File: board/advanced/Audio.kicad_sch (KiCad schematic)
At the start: 12 parts, among them J10 AudioJack3, U9 PCM5102A

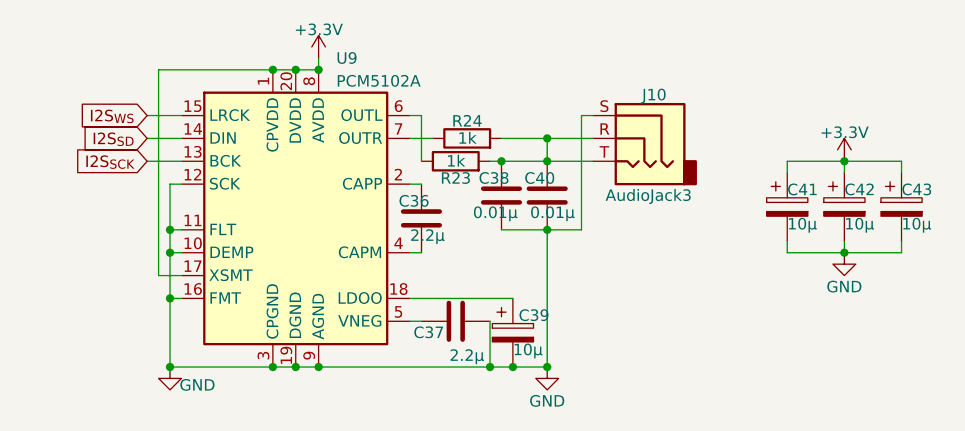
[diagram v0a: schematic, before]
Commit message: put footprints and change schematics
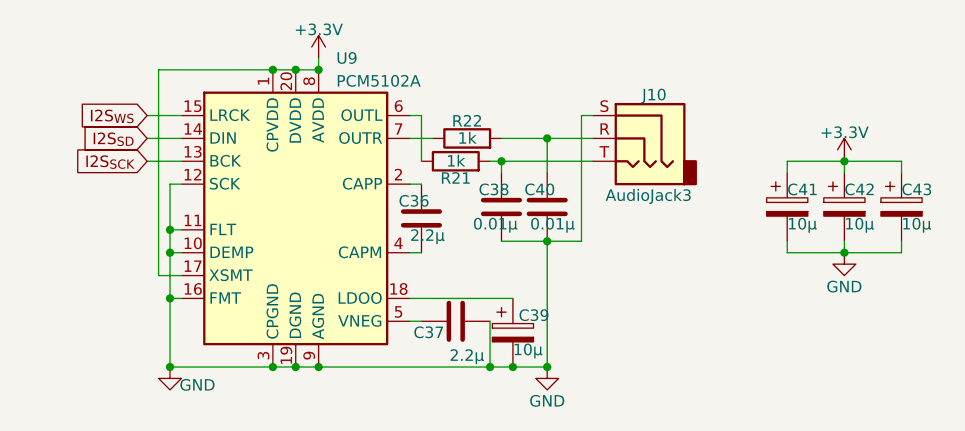
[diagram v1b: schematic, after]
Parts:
- R21: renamed from R23; footprint Resistor_SMD:R_0603_1608Metric -> Resistor_SMD:R_0402_1005Metric
- R22: renamed from R24; footprint Resistor_SMD:R_0603_1608Metric -> Resistor_SMD:R_0402_1005Metric
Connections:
- net at C40.1, J10.R, R22.2: no longer C38.1, J10.T, R21.2
- new net: C38.1, J10.T, R21.2
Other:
- moved on the sheet: C38, C40
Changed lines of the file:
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@@
-	)
-	(junction
-		(at 144.78 99.06)
-		(diameter 0)
-		(color 0 0 0 0)
 	)
 	(junction
@@
 	)
 	(junction
+		(at 144.78 107.95)
+		(diameter 0)
+		(color 0 0 0 0)
+	)
+	(junction
 		(at 114.3 88.9)
 		(diameter 0)
@@
 	)
 	(junction
-		(at 144.78 106.68)
+		(at 114.3 121.92)
+		(diameter 0)
+		(color 0 0 0 0)
+	)
+	(junction
+		(at 102.87 121.92)
+		(diameter 0)
+		(color 0 0 0 0)
+	)
+	(junction
+		(at 144.78 96.52)
 		(diameter 0)
 		(color 0 0 0 0)
@@
 	)
 	(junction
-		(at 114.3 121.92)
-		(diameter 0)
-		(color 0 0 0 0)
-	)
-	(junction
-		(at 102.87 121.92)
-		(diameter 0)
-		(color 0 0 0 0)
-	)
-	(junction
-		(at 144.78 96.52)
-		(diameter 0)
-		(color 0 0 0 0)
-	)
-	(junction
 		(at 102.87 109.22)
 		(diameter 0)
@@
 	(wire
 		(pts
-			(xy 144.78 106.68) (xy 144.78 121.92)
-		)
-		(stroke
-			(width 0)
-			(type default)
-		)
-	)
-	(wire
-		(pts
-			(xy 144.78 106.68) (xy 148.59 106.68)
+			(xy 148.59 107.95) (xy 144.78 107.95)
+		)
+		(stroke
+			(width 0)
+			(type default)
+		)
+	)
+	(wire
+		(pts
+			(xy 144.78 107.95) (xy 144.78 121.92)
 		)
 		(stroke
@@
 	(wire
 		(pts
-			(xy 148.59 93.98) (xy 148.59 106.68)
+			(xy 148.59 93.98) (xy 148.59 107.95)
 		)
 		(stroke
@@
 	(wire
 		(pts
-			(xy 144.78 99.06) (xy 149.86 99.06)
-		)
-		(stroke
-			(width 0)
-			(type default)
-		)
-	)
-	(wire
-		(pts
 			(xy 129.54 96.52) (xy 132.08 96.52)
 		)
@@
 	(wire
 		(pts
-			(xy 139.7 106.68) (xy 144.78 106.68)
+			(xy 139.7 100.33) (xy 139.7 99.06)
+		)
+		(stroke
+			(width 0)
+			(type default)
+		)
+	)
+	(wire
+		(pts
+			(xy 139.7 107.95) (xy 144.78 107.95)
 		)
 		(stroke
@@
 	(wire
 		(pts
-			(xy 139.7 99.06) (xy 144.78 99.06)
-		)
-		(stroke
-			(width 0)
-			(type default)
-		)
-	)
-	(wire
-		(pts
 			(xy 139.7 96.52) (xy 144.78 96.52)
 		)
@@
 	(wire
 		(pts
+			(xy 139.7 99.06) (xy 149.86 99.06)
+		)
+		(stroke
+			(width 0)
+			(type default)
+		)
+	)
+	(wire
+		(pts
 			(xy 101.6 111.76) (xy 104.14 111.76)
 		)
@@
 	(wire
 		(pts
-			(xy 144.78 96.52) (xy 144.78 99.06)
+			(xy 144.78 96.52) (xy 144.78 100.33)
 		)
 		(stroke
@@
 		(dnp no)
 		(fields_autoplaced yes)
-		(property "Reference" "#PWR061"
+		(property "Reference" "#PWR063"
 			(at 177.8 102.87 0)
 			(hide yes)
@@
 			(project "TurtlePico-Minimal"
 				(path "/7af2d99d-e350-48e7-86b4-20911ea922f3/c005a3df-ded2-48f6-91de-22e6372e232d"
-					(reference "#PWR061")
+					(reference "#PWR063")
 					(unit 1)
 				)
@@
 		(on_board yes)
 		(dnp no)
-		(property "Reference" "R24"
+		(property "Reference" "R22"
 			(at 135.89 94.615 90)
 			(effects
@@
 			)
 		)
-		(property "Footprint" "Resistor_SMD:R_0603_1608Metric"
+		(property "Footprint" "Resistor_SMD:R_0402_1005Metric"
 			(at 135.89 98.298 90)
 			(hide yes)
@@
 			(project "TurtlePico-Minimal"
 				(path "/7af2d99d-e350-48e7-86b4-20911ea922f3/c005a3df-ded2-48f6-91de-22e6372e232d"
-					(reference "R24")
+					(reference "R22")
 					(unit 1)
 				)
@@
 	(symbol
 		(lib_id "Device:C")
-		(at 144.78 102.87 0)
+		(at 144.78 104.14 0)
 		(unit 1)
 		(exclude_from_sim no)
@@
 		(dnp no)
 		(property "Reference" "C40"
-			(at 142.24 100.965 0)
+			(at 142.24 102.235 0)
 			(effects
 				(font
@@
 		)
 		(property "Value" "0.01µ"
-			(at 142.875 104.775 0)
+			(at 142.875 106.045 0)
 			(effects
 				(font
@@
 		)
 		(property "Footprint" "Capacitor_SMD:C_0201_0603Metric"
-			(at 145.7452 106.68 0)
+			(at 145.7452 107.95 0)
 			(hide yes)
 			(effects
@@
 		)
 		(property "Datasheet" "https://www.mouser.jp/datasheet/2/281/1/GCM188R71H103KA37_01C-3144181.pdf"
-			(at 144.78 102.87 0)
+			(at 144.78 104.14 0)
 			(hide yes)
 			(effects
@@
 		)
 		(property "Description" ""
-			(at 144.78 102.87 0)
+			(at 144.78 104.14 0)
 			(effects
 				(font
@@
 		)
 		(property "Manufacturer_Name" "Murata Electronics"
-			(at 144.78 102.87 0)
+			(at 144.78 104.14 0)
 			(hide yes)
 			(effects
@@
 		)
 		(property "Manufacturer_Part_Number" "GCM188R71H103KA37J"
-			(at 144.78 102.87 0)
+			(at 144.78 104.14 0)
 			(hide yes)
 			(effects
@@
 		)
 		(property "Mouser Part Number" "81-GCM188R71H103KA7J"
-			(at 144.78 102.87 0)
+			(at 144.78 104.14 0)
 			(hide yes)
 			(effects
@@
 		)
 		(property "Mouser Price/Stock" "https://www.mouser.jp/ProductDetail/81-GCM188R71H103KA7J"
-			(at 144.78 102.87 0)
+			(at 144.78 104.14 0)
 			(hide yes)
 			(effects
@@
 	(symbol
 		(lib_id "Device:C")
-		(at 139.7 102.87 0)
+		(at 139.7 104.14 0)
 		(unit 1)
 		(exclude_from_sim no)
@@
 		(dnp no)
 		(property "Reference" "C38"
-			(at 137.16 100.965 0)
+			(at 137.16 102.235 0)
 			(effects
 				(font
@@
 		)
 		(property "Value" "0.01µ"
-			(at 136.525 104.775 0)
+			(at 136.525 106.045 0)
 			(effects
 				(font
@@
 		)
 		(property "Footprint" "Capacitor_SMD:C_0201_0603Metric"
-			(at 140.6652 106.68 0)
+			(at 140.6652 107.95 0)
 			(hide yes)
 			(effects
@@
 		)
 		(property "Datasheet" "https://www.mouser.jp/datasheet/2/281/1/GCM188R71H103KA37_01C-3144181.pdf"
-			(at 139.7 102.87 0)
+			(at 139.7 104.14 0)
 			(hide yes)
 			(effects
@@
 		)
 		(property "Description" ""
-			(at 139.7 102.87 0)
+			(at 139.7 104.14 0)
 			(effects
 				(font
@@
 		)
 		(property "Manufacturer_Name" "Murata Electronics"
-			(at 139.7 102.87 0)
+			(at 139.7 104.14 0)
 			(hide yes)
 			(effects
@@
 		)
 		(property "Manufacturer_Part_Number" "GCM188R71H103KA37J"
-			(at 139.7 102.87 0)
+			(at 139.7 104.14 0)
 			(hide yes)
 			(effects
@@
 		)
 		(property "Mouser Part Number" "81-GCM188R71H103KA7J"
-			(at 139.7 102.87 0)
+			(at 139.7 104.14 0)
 			(hide yes)
 			(effects
@@
 		)
 		(property "Mouser Price/Stock" "https://www.mouser.jp/ProductDetail/81-GCM188R71H103KA7J"
-			(at 139.7 102.87 0)
+			(at 139.7 104.14 0)
 			(hide yes)
 			(effects
@@
 		(dnp no)
 		(fields_autoplaced yes)
-		(property "Reference" "#PWR059"
+		(property "Reference" "#PWR061"
 			(at 119.38 91.44 0)
 			(hide yes)
@@
 			(project "TurtlePico-Minimal"
 				(path "/7af2d99d-e350-48e7-86b4-20911ea922f3/c005a3df-ded2-48f6-91de-22e6372e232d"
-					(reference "#PWR059")
+					(reference "#PWR061")
 					(unit 1)
 				)
@@
 		(on_board yes)
 		(dnp no)
-		(property "Reference" "#PWR062"
+		(property "Reference" "#PWR064"
 			(at 177.8 115.57 0)
 			(hide yes)
@@
 			(project "TurtlePico-Minimal"
 				(path "/7af2d99d-e350-48e7-86b4-20911ea922f3/c005a3df-ded2-48f6-91de-22e6372e232d"
-					(reference "#PWR062")
+					(reference "#PWR064")
 					(unit 1)
 				)
@@
 		(on_board yes)
 		(dnp no)
-		(property "Reference" "#PWR060"
+		(property "Reference" "#PWR062"
 			(at 144.78 128.27 0)
 			(hide yes)
@@
 			(project "TurtlePico-Minimal"
 				(path "/7af2d99d-e350-48e7-86b4-20911ea922f3/c005a3df-ded2-48f6-91de-22e6372e232d"
-					(reference "#PWR060")
+					(reference "#PWR062")
 					(unit 1)
 				)
@@
 		(on_board yes)
 		(dnp no)
-		(property "Reference" "R23"
+		(property "Reference" "R21"
 			(at 134.62 100.965 90)
 			(effects
@@
 			)
 		)
-		(property "Footprint" "Resistor_SMD:R_0603_1608Metric"
+		(property "Footprint" "Resistor_SMD:R_0402_1005Metric"
 			(at 134.62 100.838 90)
 			(hide yes)
@@
 			(project "TurtlePico-Minimal"
 				(path "/7af2d99d-e350-48e7-86b4-20911ea922f3/c005a3df-ded2-48f6-91de-22e6372e232d"
-					(reference "R23")
+					(reference "R21")
 					(unit 1)
 				)
@@
 		(on_board yes)
 		(dnp no)
-		(property "Reference" "#PWR058"
+		(property "Reference" "#PWR060"
 			(at 102.87 128.27 0)
 			(hide yes)
@@
 			(project "TurtlePico-Minimal"
 				(path "/7af2d99d-e350-48e7-86b4-20911ea922f3/c005a3df-ded2-48f6-91de-22e6372e232d"
-					(reference "#PWR058")
+					(reference "#PWR060")
 					(unit 1)
 				)

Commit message: change schematics and complete wiring
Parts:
- C37: renamed from C36; footprint Capacitor_SMD:C_0201_0603Metric -> C_0402_1005Metric_small_pads:C_0402_1005Metric_small_pads
- C38: renamed from C37; footprint Capacitor_SMD:C_0201_0603Metric -> C_0402_1005Metric_small_pads:C_0402_1005Metric_small_pads
- C39: renamed from C38; footprint Capacitor_SMD:C_0201_0603Metric -> C_0402_1005Metric_small_pads:C_0402_1005Metric_small_pads
- C41: renamed from C40; footprint Capacitor_SMD:C_0201_0603Metric -> C_0402_1005Metric_small_pads:C_0402_1005Metric_small_pads
- R21, R22: footprint Resistor_SMD:R_0402_1005Metric -> C_0402_1005Metric_small_pads:C_0402_1005Metric_small_pads
- renumbered C39 to C40, C41 to C42, C42 to C43, C43 to C44
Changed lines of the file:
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@@
 		(on_board yes)
 		(dnp no)
-		(property "Reference" "C36"
+		(property "Reference" "C37"
 			(at 128.27 103.505 0)
 			(effects
@@
 			)
 		)
-		(property "Footprint" "Capacitor_SMD:C_0201_0603Metric"
+		(property "Footprint" "C_0402_1005Metric_small_pads:C_0402_1005Metric_small_pads"
 			(at 131.7752 109.22 0)
 			(hide yes)
@@
 			(project "TurtlePico-Minimal"
 				(path "/7af2d99d-e350-48e7-86b4-20911ea922f3/c005a3df-ded2-48f6-91de-22e6372e232d"
-					(reference "C36")
+					(reference "C37")
 					(unit 1)
 				)
@@
 		(dnp no)
 		(fields_autoplaced yes)
-		(property "Reference" "#PWR063"
+		(property "Reference" "#PWR058"
 			(at 177.8 102.87 0)
 			(hide yes)
@@
 			(project "TurtlePico-Minimal"
 				(path "/7af2d99d-e350-48e7-86b4-20911ea922f3/c005a3df-ded2-48f6-91de-22e6372e232d"
-					(reference "#PWR063")
+					(reference "#PWR058")
 					(unit 1)
 				)
@@
 			)
 		)
-		(property "Footprint" "Resistor_SMD:R_0402_1005Metric"
+		(property "Footprint" "C_0402_1005Metric_small_pads:C_0402_1005Metric_small_pads"
 			(at 135.89 98.298 90)
 			(hide yes)
@@
 		(on_board yes)
 		(dnp no)
-		(property "Reference" "C40"
+		(property "Reference" "C41"
 			(at 142.24 102.235 0)
 			(effects
@@
 			)
 		)
-		(property "Footprint" "Capacitor_SMD:C_0201_0603Metric"
+		(property "Footprint" "C_0402_1005Metric_small_pads:C_0402_1005Metric_small_pads"
 			(at 145.7452 107.95 0)
 			(hide yes)
@@
 			(project "TurtlePico-Minimal"
 				(path "/7af2d99d-e350-48e7-86b4-20911ea922f3/c005a3df-ded2-48f6-91de-22e6372e232d"
-					(reference "C40")
+					(reference "C41")
 					(unit 1)
 				)
@@
 		(on_board yes)
 		(dnp no)
-		(property "Reference" "C42"
+		(property "Reference" "C43"
 			(at 177.8 102.235 0)
 			(effects
@@
 			(project "TurtlePico-Minimal"
 				(path "/7af2d99d-e350-48e7-86b4-20911ea922f3/c005a3df-ded2-48f6-91de-22e6372e232d"
-					(reference "C42")
+					(reference "C43")
 					(unit 1)
 				)
@@
 		(on_board yes)
 		(dnp no)
-		(property "Reference" "C39"
+		(property "Reference" "C40"
 			(at 141.605 116.205 0)
 			(effects
@@
 			(project "TurtlePico-Minimal"
 				(path "/7af2d99d-e350-48e7-86b4-20911ea922f3/c005a3df-ded2-48f6-91de-22e6372e232d"
-					(reference "C39")
+					(reference "C40")
 					(unit 1)
 				)
@@
 		(on_board yes)
 		(dnp no)
-		(property "Reference" "C38"
+		(property "Reference" "C39"
 			(at 137.16 102.235 0)
 			(effects
@@
 			)
 		)
-		(property "Footprint" "Capacitor_SMD:C_0201_0603Metric"
+		(property "Footprint" "C_0402_1005Metric_small_pads:C_0402_1005Metric_small_pads"
 			(at 140.6652 107.95 0)
 			(hide yes)
@@
 			(project "TurtlePico-Minimal"
 				(path "/7af2d99d-e350-48e7-86b4-20911ea922f3/c005a3df-ded2-48f6-91de-22e6372e232d"
-					(reference "C38")
+					(reference "C39")
 					(unit 1)
 				)
@@
 		(dnp no)
 		(fields_autoplaced yes)
-		(property "Reference" "#PWR061"
+		(property "Reference" "#PWR056"
 			(at 119.38 91.44 0)
 			(hide yes)
@@
 			(project "TurtlePico-Minimal"
 				(path "/7af2d99d-e350-48e7-86b4-20911ea922f3/c005a3df-ded2-48f6-91de-22e6372e232d"
-					(reference "#PWR061")
+					(reference "#PWR056")
 					(unit 1)
 				)
@@
 		(on_board yes)
 		(dnp no)
-		(property "Reference" "#PWR064"
+		(property "Reference" "#PWR059"
 			(at 177.8 115.57 0)
 			(hide yes)
@@
 			(project "TurtlePico-Minimal"
 				(path "/7af2d99d-e350-48e7-86b4-20911ea922f3/c005a3df-ded2-48f6-91de-22e6372e232d"
-					(reference "#PWR064")
+					(reference "#PWR059")
 					(unit 1)
 				)
@@
 		(on_board yes)
 		(dnp no)
-		(property "Reference" "#PWR062"
+		(property "Reference" "#PWR057"
 			(at 144.78 128.27 0)
 			(hide yes)
@@
 			(project "TurtlePico-Minimal"
 				(path "/7af2d99d-e350-48e7-86b4-20911ea922f3/c005a3df-ded2-48f6-91de-22e6372e232d"
-					(reference "#PWR062")
+					(reference "#PWR057")
 					(unit 1)
 				)
@@
 		(on_board yes)
 		(dnp no)
-		(property "Reference" "C41"
+		(property "Reference" "C42"
 			(at 171.45 102.235 0)
 			(effects
@@
 			(project "TurtlePico-Minimal"
 				(path "/7af2d99d-e350-48e7-86b4-20911ea922f3/c005a3df-ded2-48f6-91de-22e6372e232d"
-					(reference "C41")
+					(reference "C42")
 					(unit 1)
 				)
@@
 			)
 		)
-		(property "Footprint" "Resistor_SMD:R_0402_1005Metric"
+		(property "Footprint" "C_0402_1005Metric_small_pads:C_0402_1005Metric_small_pads"
 			(at 134.62 100.838 90)
 			(hide yes)
@@
 		(on_board yes)
 		(dnp no)
-		(property "Reference" "C43"
+		(property "Reference" "C44"
 			(at 184.15 102.235 0)
 			(effects
@@
 			(project "TurtlePico-Minimal"
 				(path "/7af2d99d-e350-48e7-86b4-20911ea922f3/c005a3df-ded2-48f6-91de-22e6372e232d"
-					(reference "C43")
+					(reference "C44")
 					(unit 1)
 				)
@@
 		(on_board yes)
 		(dnp no)
-		(property "Reference" "C37"
+		(property "Reference" "C38"
 			(at 133.35 118.11 90)
 			(effects
@@
 			)
 		)
-		(property "Footprint" "Capacitor_SMD:C_0201_0603Metric"
+		(property "Footprint" "C_0402_1005Metric_small_pads:C_0402_1005Metric_small_pads"
 			(at 138.43 115.8748 0)
 			(hide yes)
@@
 			(project "TurtlePico-Minimal"
 				(path "/7af2d99d-e350-48e7-86b4-20911ea922f3/c005a3df-ded2-48f6-91de-22e6372e232d"
-					(reference "C37")
+					(reference "C38")
 					(unit 1)
 				)
@@
 		(on_board yes)
 		(dnp no)
-		(property "Reference" "#PWR060"
+		(property "Reference" "#PWR055"
 			(at 102.87 128.27 0)
 			(hide yes)
@@
 			(project "TurtlePico-Minimal"
 				(path "/7af2d99d-e350-48e7-86b4-20911ea922f3/c005a3df-ded2-48f6-91de-22e6372e232d"
-					(reference "#PWR060")
-					(unit 1)
-				)
+					(reference "#PWR055")
+					(unit 1)
+				)

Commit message: add LTB example and more
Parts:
- C37, C38: Mouser Part Number 81-GRM188R61H225KE1D -> 81-GRM155C71A225KE1J; Mouser Price/Stock https://www.mouser.jp/ProductDetail/81-GRM188R61H225KE1D -> https://www.mouser.jp/ProductDetail/Murata-Electronics/GRM1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
- C39, C41: Mouser Part Number 81-GCM188R71H103KA7J -> 81-GRM155R71C103KA1J; Mouser Price/Stock https://www.mouser.jp/ProductDetail/81-GCM188R71H103KA7J -> https://www.mouser.jp/ProductDetail/Murata-Electronics/GRM1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
- R21, R22: Mouser Part Number 660-RN73H1JT1001F100 -> 667-ERJ-2GEJ102X; Mouser Price/Stock https://www.mouser.jp/ProductDetail/660-RN73H1JT1001F100 -> https://www.mouser.jp/ProductDetail/Panasonic/ERJ-2GEJ102X?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
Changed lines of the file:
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@@
 			)
 		)
-		(property "Mouser Part Number" "81-GRM188R61H225KE1D"
+		(property "Mouser Part Number" "81-GRM155C71A225KE1J"
 			(at 130.81 105.41 0)
 			(hide yes)
@@
 			)
 		)
-		(property "Mouser Price/Stock" "https://www.mouser.jp/ProductDetail/81-GRM188R61H225KE1D"
+		(property "Mouser Price/Stock" "https://www.mouser.jp/ProductDetail/Murata-Electronics/GRM155C71A225KE11J?qs=hNud%2FORuBR2R6dsmg3BdAQ%3D%3D"
 			(at 130.81 105.41 0)
 			(hide yes)
@@
 			)
 		)
-		(property "Mouser Part Number" "660-RN73H1JT1001F100"
+		(property "Mouser Part Number" "667-ERJ-2GEJ102X"
 			(at 135.89 96.52 0)
 			(hide yes)
@@
 			)
 		)
-		(property "Mouser Price/Stock" "https://www.mouser.jp/ProductDetail/660-RN73H1JT1001F100"
+		(property "Mouser Price/Stock" "https://www.mouser.jp/ProductDetail/Panasonic/ERJ-2GEJ102X?qs=sGAEpiMZZMtG0KNrPCHnjSOOg5ypiLdnrFEbXWcegG4%3D"
 			(at 135.89 96.52 0)
 			(hide yes)
@@
 			)
 		)
-		(property "Mouser Part Number" "81-GCM188R71H103KA7J"
+		(property "Mouser Part Number" "81-GRM155R71C103KA1J"
 			(at 144.78 104.14 0)
 			(hide yes)
@@
 			)
 		)
-		(property "Mouser Price/Stock" "https://www.mouser.jp/ProductDetail/81-GCM188R71H103KA7J"
+		(property "Mouser Price/Stock" "https://www.mouser.jp/ProductDetail/Murata-Electronics/GRM155R71C103KA01J?qs=tpjTAP4gRjhDB2Lb%2FlBbPA%3D%3D"
 			(at 144.78 104.14 0)
 			(hide yes)
@@
 			)
 		)
-		(property "Mouser Part Number" "81-GCM188R71H103KA7J"
+		(property "Mouser Part Number" "81-GRM155R71C103KA1J"
 			(at 139.7 104.14 0)
 			(hide yes)
@@
 			)
 		)
-		(property "Mouser Price/Stock" "https://www.mouser.jp/ProductDetail/81-GCM188R71H103KA7J"
+		(property "Mouser Price/Stock" "https://www.mouser.jp/ProductDetail/Murata-Electronics/GRM155R71C103KA01J?qs=tpjTAP4gRjhDB2Lb%2FlBbPA%3D%3D"
 			(at 139.7 104.14 0)
 			(hide yes)
@@
 			)
 		)
-		(property "Mouser Part Number" "660-RN73H1JT1001F100"
+		(property "Mouser Part Number" "667-ERJ-2GEJ102X"
 			(at 134.62 99.06 0)
 			(hide yes)
@@
 			)
 		)
-		(property "Mouser Price/Stock" "https://www.mouser.jp/ProductDetail/660-RN73H1JT1001F100"
+		(property "Mouser Price/Stock" "https://www.mouser.jp/ProductDetail/Panasonic/ERJ-2GEJ102X?qs=sGAEpiMZZMtG0KNrPCHnjSOOg5ypiLdnrFEbXWcegG4%3D"
 			(at 134.62 99.06 0)
 			(hide yes)
@@
 			)
 		)
-		(property "Mouser Part Number" "81-GRM188R61H225KE1D"
+		(property "Mouser Part Number" "81-GRM155C71A225KE1J"
 			(at 134.62 116.84 90)
 			(hide yes)
@@
 			)
 		)
-		(property "Mouser Price/Stock" "https://www.mouser.jp/ProductDetail/81-GRM188R61H225KE1D"
+		(property "Mouser Price/Stock" "https://www.mouser.jp/ProductDetail/Murata-Electronics/GRM155C71A225KE11J?qs=hNud%2FORuBR2R6dsmg3BdAQ%3D%3D"
 			(at 134.62 116.84 90)
 			(hide yes)
